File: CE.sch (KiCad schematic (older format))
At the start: 0 parts

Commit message: Defining your inputs and outputs
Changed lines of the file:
@@
 Sheet 1 8
 Title ""
-Date "21 sep 2013"
+Date "26 sep 2013"
 Rev ""
 Comp ""
@@
 $EndDescr
 $Sheet
-S 900  1550 1850 1250
+S 2900 5050 2950 1800
 U 523D8E54
 F0 "Arduino" 50
 F1 "Arduino.sch" 50
+F2 "Relay+" O R 5850 5200 60
+F3 "Relay-" I R 5850 5300 60
+F4 "MOSI" O R 5850 5450 60
+F5 "MISO" I R 5850 5550 60
+F6 "SCLK" O R 5850 5650 60
+F7 "/CS" O R 5850 5750 60
+F8 "LED_Enable" O R 5850 5950 60
+F9 "LED_Freq" O R 5850 6100 60
+F10 "FAN_EN" O R 5850 6350 60
+F11 "Tach_Measure" I R 5850 6500 60
 $EndSheet
 $Sheet
@@
 F2 "TC IN +" I R 9550 4500 60
 F3 "TC IN -" I R 9550 4650 60
+F4 "MOSI" I L 7950 4500 60
+F5 "MISO" O L 7950 4600 60
+F6 "SCLK" I L 7950 4700 60
+F7 "/CS" I L 7950 4800 60
 $EndSheet
 $Sheet
@@
 F0 "Relay" 50
 F1 "Relay.sch" 50
+F2 "DIN+" I L 7950 5900 60
+F3 "DIN-" I L 7950 6050 60
+F4 "Relay+" I R 9550 5900 60
+F5 "Relay-" O R 9550 6050 60
 $EndSheet
 $Sheet
@@
 F0 "LED Driver" 50
 F1 "LEDDriver.sch" 50
+F2 "EN" I L 7950 1750 60
+F3 "Freq" I L 7950 1900 60
+F4 "String+" O R 9550 1750 60
+F5 "String-" I R 9550 1900 60
 $EndSheet
 $Sheet
@@
 F0 "Current Controller" 50
 F1 "CurrentController.sch" 50
+F2 "Power+" O R 9550 3050 60
+F3 "Power-" I R 9550 3200 60
+F4 "Tach" I R 9550 3350 60
+F5 "Tach_Out" O L 7950 3050 60
+F6 "Fan_In" I L 7950 3200 60
 $EndSheet
 $Sheet

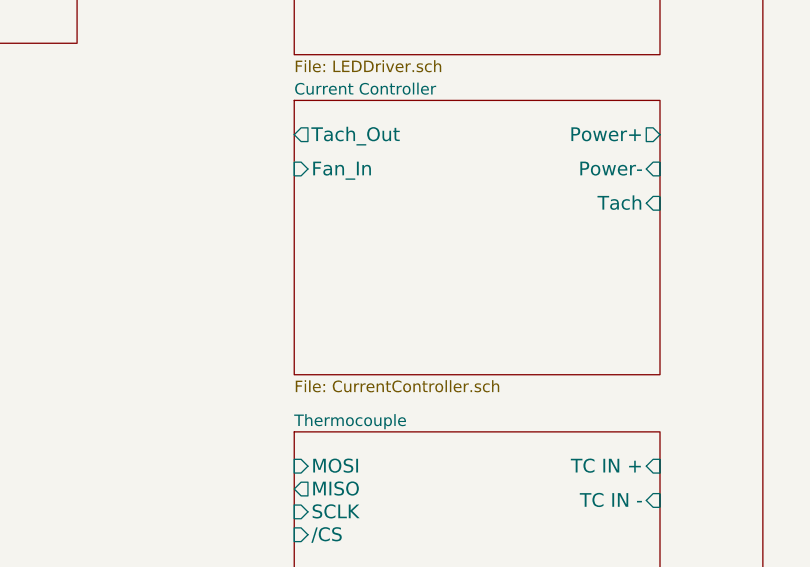
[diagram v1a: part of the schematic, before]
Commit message: understanding the current/fan driver module
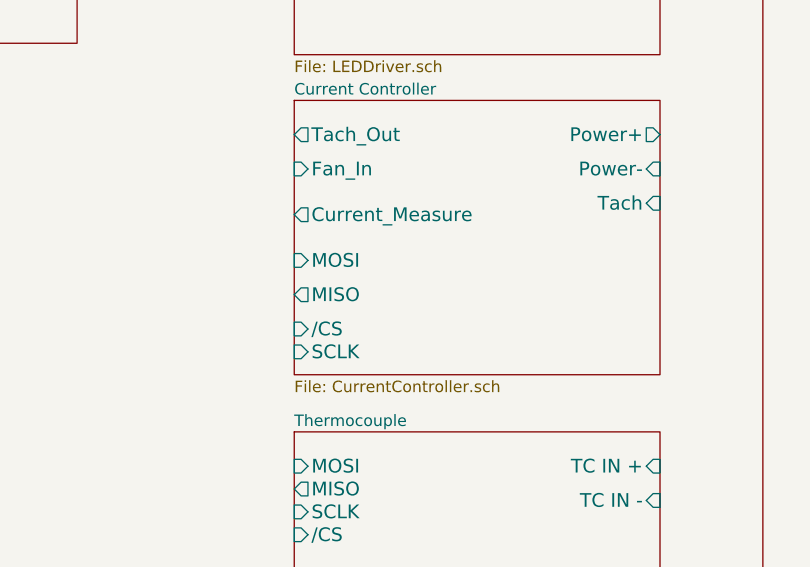
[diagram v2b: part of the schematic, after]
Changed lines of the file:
@@
 F5 "Tach_Out" O L 7950 3050 60
 F6 "Fan_In" I L 7950 3200 60
+F7 "Current_Measure" O L 7950 3400 60
+F8 "MOSI" I L 7950 3600 60
+F9 "MISO" O L 7950 3750 60
+F10 "/CS" I L 7950 3900 60
+F11 "SCLK" I L 7950 4000 60
 $EndSheet
 $Sheet

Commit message: Power protection and filtering
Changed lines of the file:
@@
 LIBS:contrib
 LIBS:valves
-LIBS:relay_spdt
+LIBS:BenchBuddy
 LIBS:CE-cache
 EELAYER 27 0
@@
 $Descr A4 11693 8268
 encoding utf-8
-Sheet 1 8
+Sheet 1 9
 Title ""
-Date "26 sep 2013"
+Date "29 sep 2013"
 Rev ""
 Comp ""
@@
 $EndSheet
 $Sheet
-S 7950 4350 1600 1100
+S 8000 5450 1650 600
 U 523D8E8D
 F0 "Thermocouple" 50
 F1 "Thermocoupe.sch" 50
-F2 "TC IN +" I R 9550 4500 60
-F3 "TC IN -" I R 9550 4650 60
-F4 "MOSI" I L 7950 4500 60
-F5 "MISO" O L 7950 4600 60
-F6 "SCLK" I L 7950 4700 60
-F7 "/CS" I L 7950 4800 60
+F2 "TC IN +" I R 9650 5600 60
+F3 "TC IN -" I R 9650 5750 60
+F4 "MOSI" I L 8000 5600 60
+F5 "MISO" O L 8000 5700 60
+F6 "SCLK" I L 8000 5800 60
+F7 "/CS" I L 8000 5900 60
 $EndSheet
 $Sheet
-S 7950 5700 1600 1050
+S 8000 6250 1650 500
 U 523D8E9D
 F0 "Relay" 50
 F1 "Relay.sch" 50
-F2 "DIN+" I L 7950 5900 60
-F3 "DIN-" I L 7950 6050 60
-F4 "Relay+" I R 9550 5900 60
-F5 "Relay-" O R 9550 6050 60
+F2 "DIN+" I L 8000 6450 60
+F3 "DIN-" I L 8000 6600 60
+F4 "Relay+" I R 9650 6450 60
+F5 "Relay-" O R 9650 6600 60
 $EndSheet
 $Sheet
@@
 $EndSheet
 $Sheet
-S 7950 1600 1600 1100
+S 8000 3400 1650 450
 U 523D8EDD
 F0 "LED Driver" 50
 F1 "LEDDriver.sch" 50
-F2 "EN" I L 7950 1750 60
-F3 "Freq" I L 7950 1900 60
-F4 "String+" O R 9550 1750 60
-F5 "String-" I R 9550 1900 60
+F2 "EN" I L 8000 3550 60
+F3 "Freq" I L 8000 3700 60
+F4 "String+" O R 9650 3550 60
+F5 "String-" I R 9650 3700 60
 $EndSheet
 $Sheet
-S 7950 2900 1600 1200
+S 8000 4050 1650 1200
 U 523D8EF5
 F0 "Current Controller" 50
 F1 "CurrentController.sch" 50
-F2 "Power+" O R 9550 3050 60
-F3 "Power-" I R 9550 3200 60
-F4 "Tach" I R 9550 3350 60
-F5 "Tach_Out" O L 7950 3050 60
-F6 "Fan_In" I L 7950 3200 60
-F7 "Current_Measure" O L 7950 3400 60
-F8 "MOSI" I L 7950 3600 60
-F9 "MISO" O L 7950 3750 60
-F10 "/CS" I L 7950 3900 60
-F11 "SCLK" I L 7950 4000 60
+F2 "Power+" O R 9650 4200 60
+F3 "Power-" I R 9650 4350 60
+F4 "Tach" I R 9650 4500 60
+F5 "Tach_Out" O L 8000 4200 60
+F6 "Fan_In" I L 8000 4350 60
+F7 "Current_Measure" O L 8000 4550 60
+F8 "MOSI" I L 8000 4750 60
+F9 "MISO" O L 8000 4900 60
+F10 "/CS" I L 8000 5050 60
+F11 "SCLK" I L 8000 5150 60
 $EndSheet
 $Sheet
-S 10000 1600 750  5200
+S 10050 650  800  6400
 U 523D8F2D
 F0 "Terminal Block" 50
 F1 "TerminalBlock.sch" 50
 $EndSheet
+$Sheet
+S 8000 2100 1650 1100
+U 52481404
+F0 "Power_Adjustment_Monitor" 50
+F1 "PowerAdjustmentMonitor.sch" 50
+F2 "V+_ADJ" O R 9650 2200 60
+F3 "V-_ADJ" O R 9650 2350 60
+F4 "3V3_MON" O L 8000 2350 60
+F5 "5V_MON" O L 8000 2200 60
+F6 "V+_ADJ_MON" O L 8000 2800 60
+F7 "V-_ADJ_MON" O L 8000 2950 60
+F8 "V+_CURR_MON" O L 8000 2500 60
+F9 "V-_CURR_MON" O L 8000 2650 60
+$EndSheet
 $EndSCHEMATC

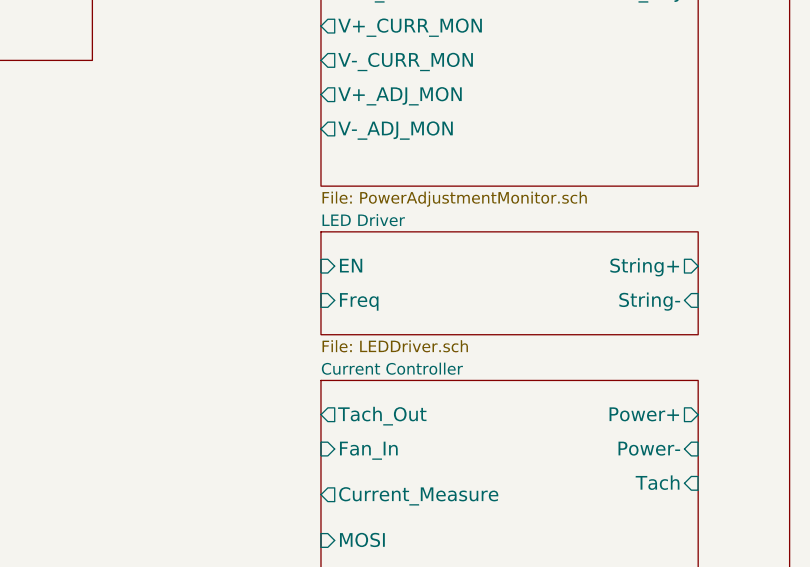
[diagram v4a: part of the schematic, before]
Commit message: LED driver model
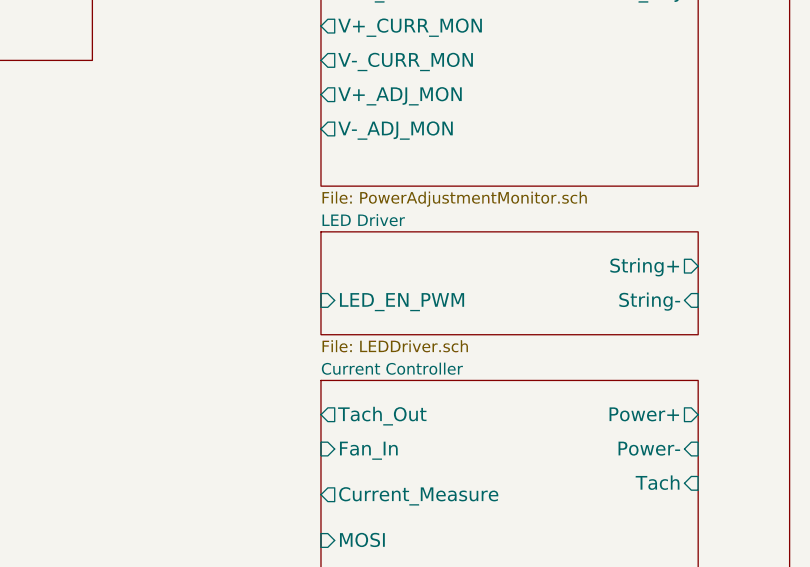
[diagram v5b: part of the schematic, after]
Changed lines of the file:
@@
 Sheet 1 9
 Title ""
-Date "29 sep 2013"
+Date "30 sep 2013"
 Rev ""
 Comp ""
@@
 F0 "LED Driver" 50
 F1 "LEDDriver.sch" 50
-F2 "EN" I L 8000 3550 60
-F3 "Freq" I L 8000 3700 60
-F4 "String+" O R 9650 3550 60
-F5 "String-" I R 9650 3700 60
+F2 "String+" O R 9650 3550 60
+F3 "String-" I R 9650 3700 60
+F4 "LED_EN_PWM" I L 8000 3700 60
 $EndSheet
 $Sheet

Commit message: Arduino Module
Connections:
- wire segments 0 -> 37
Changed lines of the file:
@@
 $EndDescr
-$Sheet
-S 2900 5050 2950 1800
-U 523D8E54
-F0 "Arduino" 50
-F1 "Arduino.sch" 50
-F2 "Relay+" O R 5850 5200 60
-F3 "Relay-" I R 5850 5300 60
-F4 "MOSI" O R 5850 5450 60
-F5 "MISO" I R 5850 5550 60
-F6 "SCLK" O R 5850 5650 60
-F7 "/CS" O R 5850 5750 60
-F8 "LED_Enable" O R 5850 5950 60
-F9 "LED_Freq" O R 5850 6100 60
-F10 "FAN_EN" O R 5850 6350 60
-F11 "Tach_Measure" I R 5850 6500 60
-$EndSheet
 $Sheet
 S 8000 5450 1650 600
@@
 F0 "Relay" 50
 F1 "Relay.sch" 50
-F2 "DIN+" I L 8000 6450 60
-F3 "DIN-" I L 8000 6600 60
-F4 "Relay+" I R 9650 6450 60
-F5 "Relay-" O R 9650 6600 60
+F2 "RELAY_NC" B R 9650 6350 60
+F3 "RELAY_NO" B R 9650 6500 60
+F4 "RELAY_COM" B R 9650 6650 60
+F5 "RELAY+" I L 8000 6400 60
+F6 "RELAY-" I L 8000 6600 60
 $EndSheet
 $Sheet
@@
 F0 "LED Driver" 50
 F1 "LEDDriver.sch" 50
-F2 "String+" O R 9650 3550 60
-F3 "String-" I R 9650 3700 60
-F4 "LED_EN_PWM" I L 8000 3700 60
-$EndSheet
-$Sheet
-S 8000 4050 1650 1200
-U 523D8EF5
-F0 "Current Controller" 50
-F1 "CurrentController.sch" 50
-F2 "Power+" O R 9650 4200 60
-F3 "Power-" I R 9650 4350 60
-F4 "Tach" I R 9650 4500 60
-F5 "Tach_Out" O L 8000 4200 60
-F6 "Fan_In" I L 8000 4350 60
-F7 "Current_Measure" O L 8000 4550 60
-F8 "MOSI" I L 8000 4750 60
-F9 "MISO" O L 8000 4900 60
-F10 "/CS" I L 8000 5050 60
-F11 "SCLK" I L 8000 5150 60
+F2 "LED_EN_PWM" I L 8000 3700 60
+F3 "LED_STRING+" O R 9650 3550 60
+F4 "LED_STRING-" I R 9650 3700 60
 $EndSheet
 $Sheet
@@
 F0 "Terminal Block" 50
 F1 "TerminalBlock.sch" 50
+F2 "V+_ADJ" I L 10050 2200 60
+F3 "V-_ADJ" I L 10050 2350 60
+F4 "FAN_OUT+" O L 10050 4200 60
+F5 "FAN_OUT-" O L 10050 4350 60
+F6 "TACH_IN" I L 10050 5100 60
+F7 "LED_STRING+" O L 10050 3550 60
+F8 "LED_STRING-" O L 10050 3700 60
+F9 "TC_IN+" I L 10050 5600 60
+F10 "TC_IN-" I L 10050 5750 60
+F11 "RELAY_COM" B L 10050 6650 60
+F12 "RELAY_NO" B L 10050 6500 60
+F13 "RELAY_NC" B L 10050 6350 60
 $EndSheet
 $Sheet
@@
 F9 "V-_CURR_MON" O L 8000 2650 60
 $EndSheet
+$Sheet
+S 8000 4050 1650 1200
+U 523D8EF5
+F0 "Current Controller" 50
+F1 "CurrentController.sch" 50
+F2 "MOSI" I L 8000 4700 60
+F3 "MISO" O L 8000 4850 60
+F4 "/CS" I L 8000 5000 60
+F5 "SCLK" I L 8000 5150 60
+F6 "FAN_OUT+" O R 9650 4200 60
+F7 "TACH_IN" I R 9650 5100 60
+F8 "TACH_MEAS" O L 8000 4550 60
+F9 "/FAN_EN" I L 8000 4400 60
+F10 "CURR_MEAS" O L 8000 4250 60
+F11 "FAN_OUT-" O R 9650 4350 60
+$EndSheet
+Wire Wire Line
+	10050 2200 9650 2200
+Wire Wire Line
+	9650 2350 10050 2350
+Wire Wire Line
+	10050 3550 9650 3550
+Wire Wire Line
+	9650 3700 10050 3700
+Wire Wire Line
+	10050 4200 9650 4200
+Wire Wire Line
+	9650 4350 10050 4350
+Wire Wire Line
+	10050 5100 9650 5100
+Wire Wire Line
+	9650 5600 10050 5600
+Wire Wire Line
+	10050 5750 9650 5750
+Wire Wire Line
+	9650 6350 10050 6350
+Wire Wire Line
+	10050 6500 9650 6500
+Wire Wire Line
+	9650 6650 10050 6650
+$Sheet
+S 3900 3700 3000 3050
+U 523D8E54
+F0 "Arduino" 50
+F1 "Arduino.sch" 50
+F2 "MOSI" O R 6900 4700 60
+F3 "MISO" I R 6900 4850 60
+F4 "SCLK" O R 6900 5150 60
+F5 "RELAY+" O R 6900 6400 60
+F6 "RELAY-" I R 6900 6600 60
+F7 "LED_EN_PWM" O R 6900 4100 60
+F8 "/FAN_EN" O R 6900 4400 60
+F9 "TACH_MEAS" I R 6900 4550 60
+F10 "CURR_MEAS" I R 6900 4250 60
+F11 "V+_ADJ_MON" I R 6900 3800 60
+F12 "V-_ADJ_MON" I R 6900 3950 60
+F13 "/CS_FAN" O R 6900 5000 60
+F14 "/CS_TC" O R 6900 5900 60
+$EndSheet
+Wire Wire Line
+	6850 3800 7350 3800
+Wire Wire Line
+	7350 3800 7350 2800
+Wire Wire Line
+	7350 2800 8000 2800
+Wire Wire Line
+	8000 2950 7500 2950
+Wire Wire Line
+	7500 2950 7500 3950
+Wire Wire Line
+	7500 3950 6850 3950
+Wire Wire Line
+	6850 4700 8000 4700
+Wire Wire Line
+	8000 4850 6850 4850
+Wire Wire Line
+	6850 5150 8000 5150
+Wire Wire Line
+	6850 4550 8000 4550
+Wire Wire Line
+	6850 4400 8000 4400
+Wire Wire Line
+	6850 4250 8000 4250
+Wire Wire Line
+	6850 4100 7650 4100
+Wire Wire Line
+	7650 4100 7650 3700
+Wire Wire Line
+	7650 3700 8000 3700
+Wire Wire Line
+	6900 6400 8000 6400
+Wire Wire Line
+	8000 6600 6900 6600
+Wire Wire Line
+	7300 4700 7300 5600
+Wire Wire Line
+	7300 5600 8000 5600
+Connection ~ 7300 4700
+Wire Wire Line
+	8000 5700 7200 5700
+Wire Wire Line
+	7200 5700 7200 4850
+Connection ~ 7200 4850
+Wire Wire Line
+	7100 5150 7100 5800
+Wire Wire Line
+	7100 5800 8000 5800
+Connection ~ 7100 5150
+Wire Wire Line
+	6900 5000 8000 5000
+Wire Wire Line
+	6900 5900 8000 5900
 $EndSCHEMATC
